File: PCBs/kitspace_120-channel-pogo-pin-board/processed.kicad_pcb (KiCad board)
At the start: 4 copper layers, 108.2 x 73.2 mm, 17 parts, among them J4 SFM-120-02-L-D-A, J5 SFM-125-02-L-D-A, J6 SFM-120-02-L-D-A, P1 Conn_02x17_Odd_Even, P2 Conn_02x17_Odd_Even, P3 Conn_02x17_Odd_Even, P4 Conn_02x17_Odd_Even, P5 CONN_01X01, P6 CONN_01X01, P7 CONN_01X01, P8 CONN_01X01, U1 CAT24C02TDI

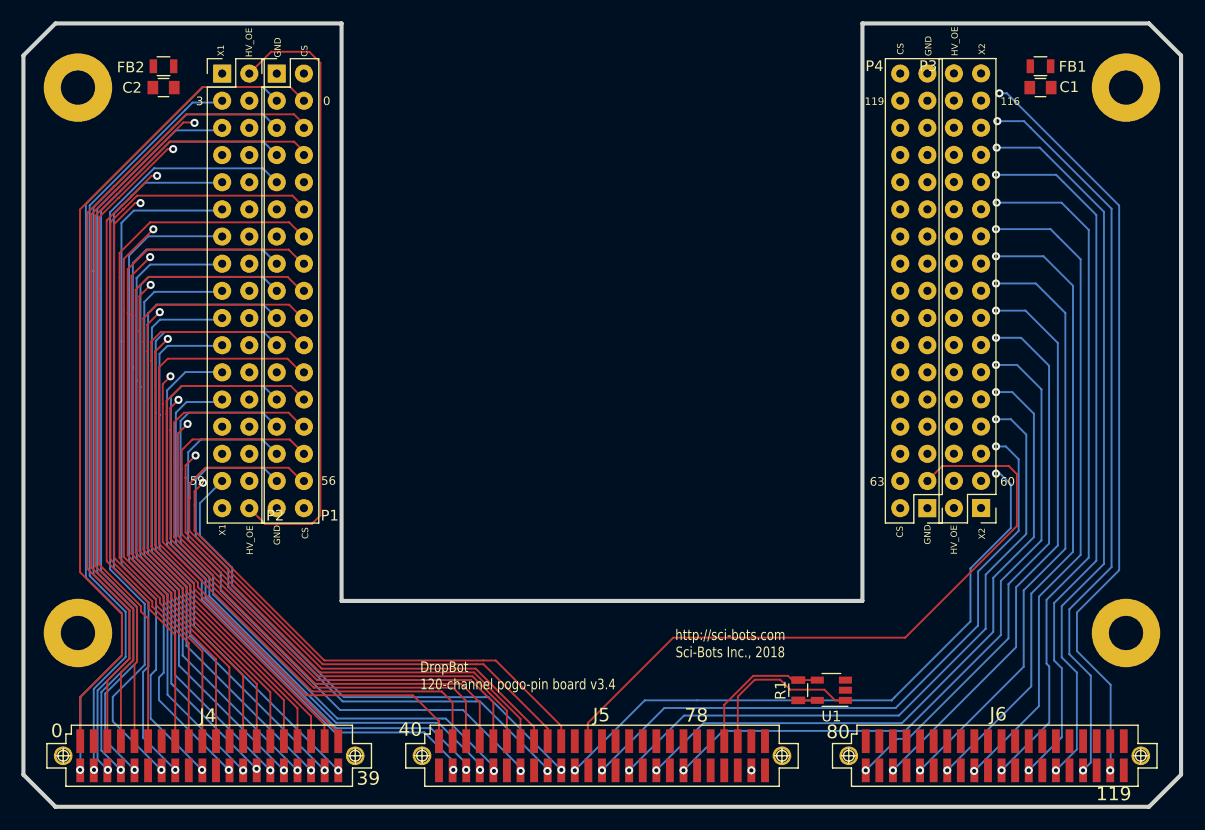
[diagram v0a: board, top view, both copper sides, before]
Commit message: recheck all circuits and clean up fill zone by rerouting the nets using freerouting and manually
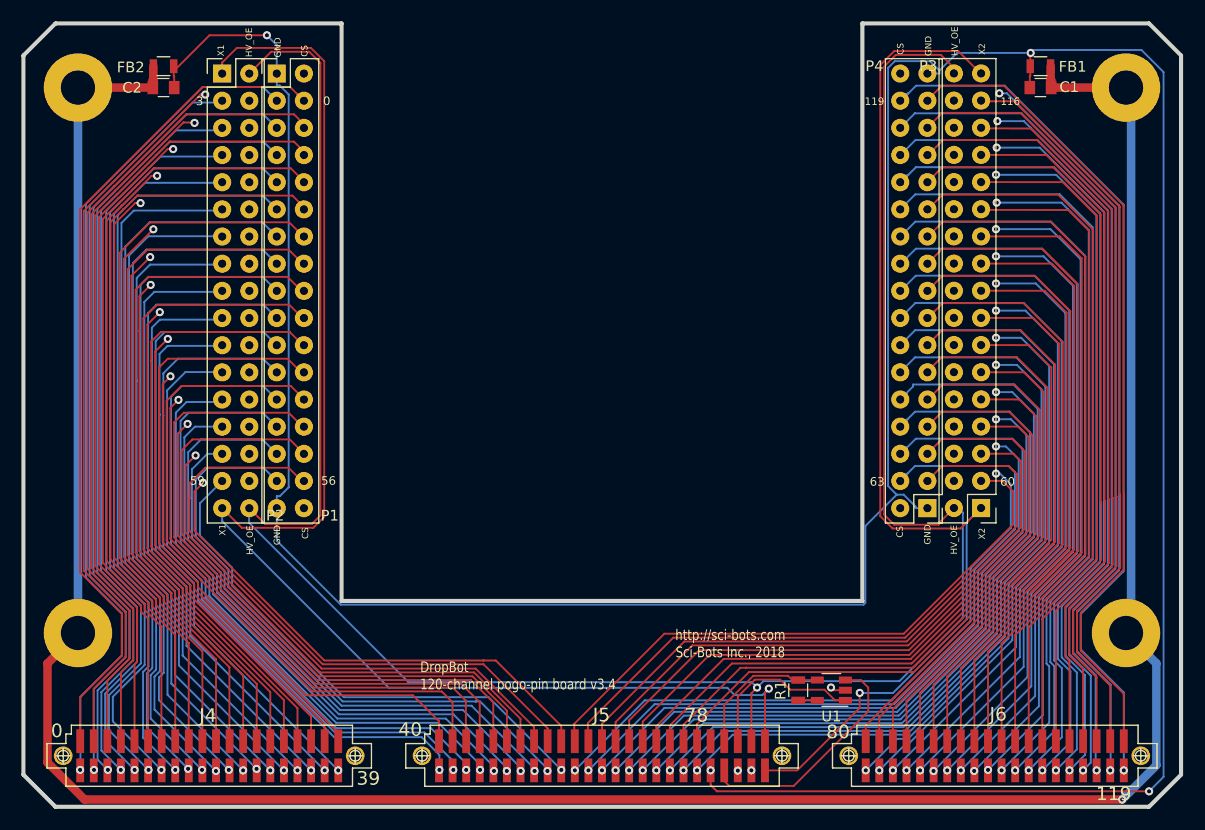
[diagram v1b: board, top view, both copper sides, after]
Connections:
- C1 pad 1: (no net) -> GND
- C1 pad 2: (no net) -> CHASIS_GND
- C2 pad 1: (no net) -> GND
- C2 pad 2: (no net) -> CHASIS_GND
- FB1 pad 1: (no net) -> GND
- FB1 pad 2: (no net) -> CHASIS_GND
- FB2 pad 1: (no net) -> GND
- FB2 pad 2: (no net) -> CHASIS_GND
- J4 pad 1: (no net) -> CH39
- J4 pad 11: (no net) -> CH29
- J4 pad 15: (no net) -> CH25
- J4 pad 19: (no net) -> CH21
- J4 pad 23: (no net) -> CH17
- J4 pad 28: (no net) -> CH12
- J4 pad 3: (no net) -> CH37
- J4 pad 38: (no net) -> CH2
- J4 pad 5: (no net) -> CH35
- J4 pad 7: (no net) -> CH33
- J4 pad 9: (no net) -> CH31
- J5 pad 1: (no net) -> CH-X2
- J5 pad 10: (no net) -> +12V
- J5 pad 11: (no net) -> CH79
- J5 pad 12: (no net) -> CH78
- J5 pad 13: (no net) -> CH77
- J5 pad 14: (no net) -> CH76
- J5 pad 15: (no net) -> CH75
- J5 pad 16: (no net) -> CH74
- J5 pad 17: (no net) -> CH73
- J5 pad 18: (no net) -> CH72
- J5 pad 19: (no net) -> CH71
- J5 pad 2: (no net) -> CH-X1
- J5 pad 20: (no net) -> CH70
- J5 pad 21: (no net) -> CH69
- J5 pad 22: (no net) -> CH68
- J5 pad 23: (no net) -> CH67
- J5 pad 24: (no net) -> CH66
- J5 pad 25: (no net) -> CH65
- J5 pad 26: (no net) -> CH64
- J5 pad 27: (no net) -> CH63
- J5 pad 29: (no net) -> CH61
- J5 pad 3: (no net) -> CUR_SENSE
- J5 pad 30: (no net) -> CH60
- J5 pad 35: (no net) -> CH55
- J5 pad 39: (no net) -> CH51
- J5 pad 4: (no net) -> HV_OE
- J5 pad 49: (no net) -> CH41
- J5 pad 5: (no net) -> GND
- J5 pad 7: (no net) -> SDA
- J5 pad 9: (no net) -> GND
- J6 pad 1: (no net) -> CH119
- J6 pad 10: (no net) -> CH110
- J6 pad 11: (no net) -> CH109
- J6 pad 12: (no net) -> CH108
- J6 pad 13: (no net) -> CH107
- J6 pad 14: (no net) -> CH106
- J6 pad 15: (no net) -> CH105
- J6 pad 16: (no net) -> CH104
- J6 pad 17: (no net) -> CH103
- J6 pad 18: (no net) -> CH102
- J6 pad 19: (no net) -> CH101
- J6 pad 2: (no net) -> CH118
- J6 pad 20: (no net) -> CH100
- J6 pad 21: (no net) -> CH99
- J6 pad 22: (no net) -> CH98
- J6 pad 24: (no net) -> CH96
- J6 pad 25: (no net) -> CH95
- J6 pad 26: (no net) -> CH94
- J6 pad 27: (no net) -> CH93
- J6 pad 28: (no net) -> CH92
- J6 pad 29: (no net) -> CH91
- J6 pad 3: (no net) -> CH117
- J6 pad 30: (no net) -> CH90
- J6 pad 31: (no net) -> CH89
- J6 pad 32: (no net) -> CH88
- J6 pad 33: (no net) -> CH87
- J6 pad 34: (no net) -> CH86
- J6 pad 35: (no net) -> CH85
- J6 pad 36: (no net) -> CH84
- J6 pad 37: (no net) -> CH83
- J6 pad 38: (no net) -> CH82
- J6 pad 39: (no net) -> CH81
- J6 pad 4: (no net) -> CH116
- J6 pad 40: (no net) -> CH80
- J6 pad 5: (no net) -> CH115
- J6 pad 6: (no net) -> CH114
- J6 pad 7: (no net) -> CH113
- J6 pad 8: (no net) -> CH112
- J6 pad 9: (no net) -> CH111
- P1 pad 1: (no net) -> GND
- P1 pad 10: (no net) -> CH12
- P1 pad 11: (no net) -> CH17
- P1 pad 13: (no net) -> CH21
- P1 pad 23: (no net) -> CH41
- P1 pad 33: (no net) -> GND
- P2 pad 1: (no net) -> CH-X1
- P2 pad 27: (no net) -> CH51
- P2 pad 29: (no net) -> CH55
- P2 pad 33: (no net) -> CH-X1
- P2 pad 4: (no net) -> CH2
- P2 pad 7: (no net) -> CH11
- P3 pad 1: (no net) -> CH-X2
- P3 pad 11: (no net) -> CH76
- P3 pad 13: (no net) -> CH80
- P3 pad 15: (no net) -> CH84
- P3 pad 17: (no net) -> CH88
- P3 pad 19: (no net) -> CH92
- P3 pad 2: (no net) -> HV_OE
- P3 pad 21: (no net) -> CH96
- P3 pad 23: (no net) -> CH100
- P3 pad 25: (no net) -> CH104
- P3 pad 27: (no net) -> CH108
- P3 pad 29: (no net) -> CH112
- P3 pad 3: (no net) -> CH60
- P3 pad 31: (no net) -> CH116
- P3 pad 33: (no net) -> CH-X2
- P3 pad 34: (no net) -> HV_OE
- P3 pad 5: (no net) -> CH64
- P3 pad 7: (no net) -> CH68
- P3 pad 9: (no net) -> CH72
- P4 pad 1: (no net) -> GND
- P4 pad 10: (no net) -> CH75
- P4 pad 11: (no net) -> CH78
- P4 pad 12: (no net) -> CH79
- P4 pad 13: (no net) -> CH82
- P4 pad 14: (no net) -> CH83
- P4 pad 15: (no net) -> CH86
- P4 pad 16: (no net) -> CH87
- P4 pad 17: (no net) -> CH90
- P4 pad 18: (no net) -> CH91
- P4 pad 19: (no net) -> CH94
- P4 pad 2: (no net) -> CUR_SENSE
- P4 pad 20: (no net) -> CH95
- P4 pad 21: (no net) -> CH98
- P4 pad 22: (no net) -> CH99
- P4 pad 23: (no net) -> CH102
- P4 pad 24: (no net) -> CH103
- P4 pad 25: (no net) -> CH106
- P4 pad 26: (no net) -> CH107
- P4 pad 27: (no net) -> CH110
- P4 pad 28: (no net) -> CH111
- P4 pad 29: (no net) -> CH114
- P4 pad 30: (no net) -> CH115
- P4 pad 31: (no net) -> CH118
- P4 pad 32: (no net) -> CH119
- P4 pad 33: (no net) -> GND
- P4 pad 34: (no net) -> CUR_SENSE
- P4 pad 4: (no net) -> CH63
- P4 pad 5: (no net) -> CH66
- P4 pad 6: (no net) -> CH67
- P4 pad 7: (no net) -> CH70
- P4 pad 8: (no net) -> CH71
- P4 pad 9: (no net) -> CH74
- P5 pad 1: (no net) -> CHASIS_GND
- P6 pad 1: (no net) -> CHASIS_GND
- U1 pad 2: (no net) -> GND
- U1 pad 3: (no net) -> SDA
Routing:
- net GND: track 0.00 -> 332.7 mm, vias 0 -> 6
- net HV_OE: track 57.8 -> 209.7 mm, vias 0 -> 1
- net CH-X1: track 0.00 -> 129.9 mm, vias 0 -> 1
- net CHASIS_GND: track 134.8 -> 253.7 mm, vias 0 -> 1
- net CH-X2: track 0.00 -> 101.3 mm, vias 0 -> 1
- net CH119: track 0.00 -> 83.3 mm, vias 0 -> 1
- net CH115: track 0.00 -> 79.5 mm, vias 0 -> 1
- net CH118: track 0.00 -> 78.1 mm
- net CH111: track 0.00 -> 78.1 mm, vias 0 -> 1
- net CH107: track 0.00 -> 77.4 mm, vias 0 -> 1
- net CH114: track 0.00 -> 75.4 mm
- net CH2: track 0.00 -> 74.6 mm, vias 0 -> 1
- net CH79: track 0.00 -> 74.3 mm, vias 0 -> 1
- net CH103: track 0.00 -> 74.0 mm, vias 0 -> 1
- net CH75: track 0.00 -> 73.8 mm, vias 0 -> 1
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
